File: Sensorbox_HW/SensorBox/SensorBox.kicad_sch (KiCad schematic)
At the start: 62 parts, among them Q1 BSS83P, SW1 SW_SPST, U1 BME280, U10 TLV2371D, U12 DS3231M, U2 LT1054, U3 PS1-O3-100, U4 MC33063AD, U6 MAX31855EASA, U8 HPP845E131R5, U9 TLV2371D

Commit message: Überarbeitung Sensorbox V3
Sicherheitsschaltung eingebaut, ESP anschauen warum getauscht, Email geschrieben
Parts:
- removed F1: Fuse, Fuse:Fuseholder_TR5_Littelfuse_No560_No460, symbol Device:Fuse
- removed SW1: SW_SPST, Button_Switch_THT:SW_SPST_Omron_B3F-40xx, symbol Switch:SW_SPST
- added LED1, LED2: rt, symbol Device:LED
- added Q2, Q3: BC327, Package_TO_SOT_THT:TO-92_Inline, symbol Transistor_BJT:BC327
- added R21, R22, R23: 1k, Resistor_SMD:R_0402_1005Metric, symbol Device:R
- added Rm: 5R, Resistor_SMD:R_0402_1005Metric, symbol Device:R
- MicroSD2: footprint (none) -> Connector_Card:microSD_HC_Molex_104031-0811
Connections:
- net GND1: no longer BT1.-
- net VCC_Bat: now also LED2.2 (A), Q2.1 (C)
- net at BT1.+: now also Q3.3 (E), Rm.2
- new net: BT1.-, R22.2, R23.2
- new net: LED1.2 (A), Q2.2 (B)
- new net: Q2.3 (E), R21.1, Rm.1
- new net: LED2.1 (K), R23.1
- new net: LED1.1 (K), Q3.1 (C), R22.1
- new net: Q3.2 (B), R21.2
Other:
- note added: "1V5 3x4V5 + Sicherung"
- note added: "RM = VBE/Ischwelle Rm=0,7V/0,140A =~5R"
- note added: "Sicherung +"
- note added: "Sicherung -"
- note removed: "1V5 3x 4V5"
- moved on the sheet: BT1, C1, C2, C3, C4, C5, C7, C8, CO1, CO2, CO3, CR1220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

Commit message: Überarbeitung V3
Besprechung mit B2 und einige Dinge Überarbeitet (Fuse, SD Card usw.)
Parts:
- removed JP2, JP3: Jumper_3_Bridged12, Connector_PinHeader_2.54mm:PinHeader_1x03_P2.54mm_Vertical, symbol Jumper:Jumper_3_Bridged12
- removed LED1, LED2: rt, symbol Device:LED
- removed Pulldown_Max2, Pulldown_Max318551, R1: 10k, Resistor_SMD:R_0402_1005Metric, symbol Device:R
- removed Q2, Q3: BC327, Package_TO_SOT_THT:TO-92_Inline, symbol Transistor_BJT:BC327
- removed R10, R9: 4.7k, Resistor_SMD:R_0402_1005Metric, symbol Device:R
- removed R16, R17, R18, R21, R22, R23: 1k, Resistor_SMD:R_0402_1005Metric, symbol Device:R
- removed Rm: 5R, Resistor_SMD:R_0402_1005Metric, symbol Device:R
- added ADC, GND1, SCL1, SDA/Signal1, VCC1: Conn_01x01_Socket, Connector_PinHeader_2.00mm:PinHeader_1x01_P2.00mm_Vertical, symbol Connector:Conn_01x01_Socket
- added C9: 100nF, Capacitor_SMD:C_0402_1005Metric_Pad0.74x0.62mm_HandSolder, symbol Device:C
- added D2, D3, D4: 1.5KExxA, Diode_THT:D_DO-201AE_P15.24mm_Horizontal, symbol Diode:1.5KExxA
- added F1: Polyfuse_Small, symbol Device:Polyfuse_Small
- added JP1: Jumper_2_Bridged, symbol Jumper:Jumper_2_Bridged
- CO2: value 00µF -> 10µF
- R19: value 2.2k -> 1k
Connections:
- net CS_GPIO5: now also MicroSD2.2 (CS), R21.1
- net GND1: now also BT1.-, U1.5 (SDO), C9.2, D2.2 (A2), D3.2 (A2), D4.2 (A2), GND1.1 (Pin_1); no longer R19.2, R20.2, R21.2, R7.2, R8.2
- net Mosi_GPIO23: now also MicroSD2.3 (DI), R20.1
- net RTC_32Khz_GPIO32: now also U7.5 (34); no longer U7.2 (EN)
- net SCK_GPIO18: now also MicroSD2.5 (SCK), R19.1
- net SCL_GPIO22: now also D2.1 (A1), SCL1.1 (Pin_1)
- net SDA_GPIO21: now also D4.1 (A1), SDA/Signal1.1 (Pin_1)
- net VCC_Bat: now also F1.2
- net VDD_3V3: now also R19.2, R20.2, R21.2, R7.2, R8.2; no longer U1.5 (SDO)
- net VDD_5V: now also C9.1, VCC1.1 (Pin_1)
- net at BT1.+: now also D3.1 (A1), F1.1
- net at U6.2 (T-): now also TH2.1, JP1.1 (A)
- net at TH2.2: now also U6.3 (T+), JP1.2 (B)
- net extern_Sensor_Gpio_32: now reaches U7.8 (33)
- net extern_Sensor_Gpio_32: now also ADC.1 (Pin_1)
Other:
- note added: "IoutMax bei -5V -> 100mA"
- note added: "Luftdruck-Sensor"
- note added: "Luftfeuchtigkeits-Sensor"
- note added: "Steckpins für den externen Sensor"
- note added: "Wichtig fürs Layout: Der Sensor der am Schluss der Datenleitung hängt Pullup Widerstände hängen. Hier BME!!!"
- note added: "für 3,3V"
- note removed: "BME280-Sensor"
- note removed: "Dauer --> P_BAT / P_Verbrauch = 46.06h"
- note removed: "HPP845E131R5-Sensor"
- note removed: "IoutMax bei -5V = 100mA"
- note removed: "P_Verbrauch = 0.122Wh"
- note removed: "RM = VBE/Ischwelle Rm=0,7V/0,140A =~5R"
- note removed: "Sicherung +"
- note removed: "Sicherung -"
- moved on the sheet: BT1

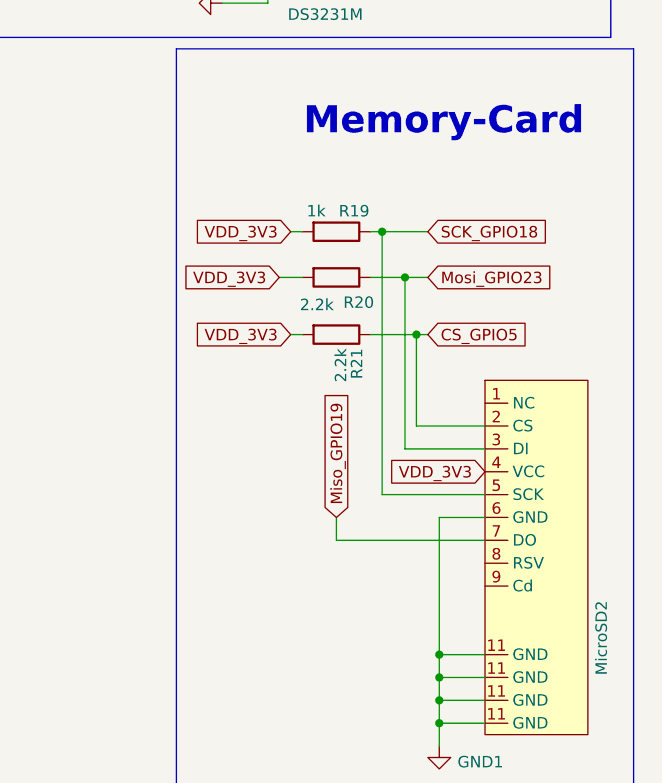
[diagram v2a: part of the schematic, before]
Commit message: Besprechung B2
Sicherung noch zu Datenleitungen dazu gehängt
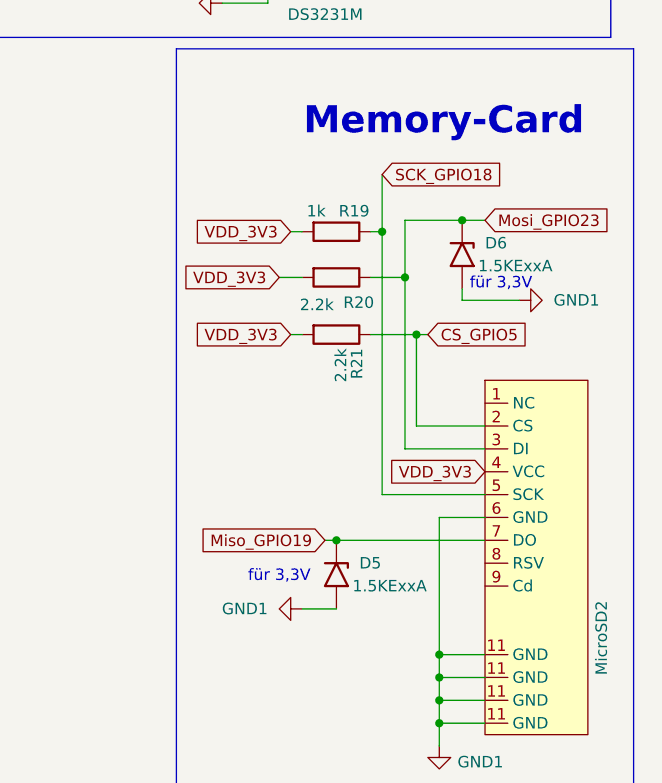
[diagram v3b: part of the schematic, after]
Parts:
- added D5, D6: 1.5KExxA, Diode_THT:D_DO-201AE_P15.24mm_Horizontal, symbol Diode:1.5KExxA
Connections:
- net GND1: now also D5.2 (A2), D6.2 (A2)
- net Miso_GPIO19: now also D5.1 (A1)
- net Mosi_GPIO23: now also D6.1 (A1)

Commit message: test
test
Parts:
- R19: value 1k -> 3k
- R20, R21: value 2.2k -> 3k
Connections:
- net RTC_32Khz_GPIO32 renamed RTC_32Khz_GPIO34
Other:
- note added: "Passt"
- note added: "Passt nicht"
- note added: "Passt nicht - EPAD anschauen ob es nötig ist"
- note added: "Passt nicht wegen Pin1"
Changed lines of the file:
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@@
 		)
 	)
+	(text "Passt"
+		(exclude_from_sim no)
+		(at 66.04 225.044 0)
+		(effects
+			(font
+				(size 2.032 2.032)
+				(thickness 0.4064)
+				(bold yes)
+			)
+		)
+	)
 	(text "Spannungsregler -- 3V-40V Input, Output\neinstellbar, hier indem Fall 5V"
 		(exclude_from_sim no)
@@
 		)
 	)
+	(text "Passt"
+		(exclude_from_sim no)
+		(at 268.732 172.72 0)
+		(effects
+			(font
+				(size 1.27 1.27)
+				(bold yes)
+			)
+		)
+	)
+	(text "Passt nicht wegen Pin1"
+		(exclude_from_sim no)
+		(at 387.35 52.07 0)
+		(effects
+			(font
+				(size 1.27 1.27)
+				(bold yes)
+			)
+		)
+	)
 	(text "für 3,3V\n"
 		(exclude_from_sim no)
@@
 		)
 	)
+	(text "Passt"
+		(exclude_from_sim no)
+		(at 196.596 24.384 0)
+		(effects
+			(font
+				(size 2.032 2.032)
+				(thickness 0.4064)
+				(bold yes)
+			)
+		)
+	)
 	(text "IoutMax bei -5V -> 100mA\n"
 		(exclude_from_sim no)
@@
 		)
 	)
+	(text "Passt\n"
+		(exclude_from_sim no)
+		(at 248.412 150.876 0)
+		(effects
+			(font
+				(size 1.27 1.27)
+				(bold yes)
+			)
+		)
+	)
 	(text "Spannungs Inverter\n"
 		(exclude_from_sim no)
@@
 		)
 	)
+	(text "Passt nicht "
+		(exclude_from_sim no)
+		(at 366.522 143.002 0)
+		(effects
+			(font
+				(size 1.27 1.27)
+				(bold yes)
+			)
+		)
+	)
+	(text "Passt nicht - EPAD anschauen \nob es nötig ist"
+		(exclude_from_sim no)
+		(at 135.89 179.578 0)
+		(effects
+			(font
+				(size 1.27 1.27)
+				(bold yes)
+			)
+		)
+	)
 	(text "Ozon-Sensor"
 		(exclude_from_sim no)
@@
 		)
 	)
+	(text "Passt nicht"
+		(exclude_from_sim no)
+		(at 176.276 175.26 0)
+		(effects
+			(font
+				(size 1.27 1.27)
+				(bold yes)
+			)
+		)
+	)
+	(text "Passt"
+		(exclude_from_sim no)
+		(at 175.26 88.9 0)
+		(effects
+			(font
+				(size 2.032 2.032)
+				(thickness 0.4064)
+				(bold yes)
+			)
+		)
+	)
 	(global_label "VDD_3V3"
 		(shape input)
@@
 		)
 	)
-	(global_label "RTC_32Khz_GPIO32"
+	(global_label "RTC_32Khz_GPIO34"
 		(shape input)
 		(at 255.27 39.37 180)
@@
 		)
 	)
-	(global_label "RTC_32Khz_GPIO32"
+	(global_label "RTC_32Khz_GPIO34"
 		(shape input)
 		(at 378.46 35.56 0)
@@
 			)
 		)
-		(property "Value" "2.2k"
+		(property "Value" "3k"
 			(at 365.506 85.598 90)
 			(effects
@@
 			)
 		)
-		(property "Value" "1k"
+		(property "Value" "3k"
 			(at 366.268 75.184 90)
 			(effects
@@
 			)
 		)
-		(property "Value" "2.2k"
+		(property "Value" "3k"
 			(at 370.078 90.424 0)
 			(effects

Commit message: SensorboxV4
Fertigstellen
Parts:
- removed C3, C7: 100nF, Capacitor_SMD:C_0402_1005Metric_Pad0.74x0.62mm_HandSolder, symbol Device:C
- removed CO1: 2µF, Capacitor_SMD:C_0402_1005Metric_Pad0.74x0.62mm_HandSolder, symbol Device:C
- removed CO2: 10µF, Capacitor_SMD:C_0402_1005Metric_Pad0.74x0.62mm_HandSolder, symbol Device:C
- removed CO3: 100µF, Capacitor_SMD:C_0402_1005Metric_Pad0.74x0.62mm_HandSolder, symbol Device:C
- removed Q1: BSS83P, Package_TO_SOT_SMD:SOT-23, symbol Transistor_FET:BSS83P
- removed R11, R2, R3: 10k, Resistor_SMD:R_0402_1005Metric, symbol Device:R
- removed R4, R5: 10R, Resistor_SMD:R_0402_1005Metric, symbol Device:R
- removed R6: 100k, Resistor_SMD:R_0402_1005Metric, symbol Device:R
- removed RGain: 82k, Resistor_SMD:R_0402_1005Metric, symbol Device:R
- removed U10, U9: TLV2371D, Package_SO:SOIC-8_3.9x4.9mm_P1.27mm, symbol Amplifier_Operational:TLV2371D
- removed U2: LT1054, symbol Regulator_SwitchedCapacitor:LT1054
- removed U3: PS1-O3-100, PS1O3100, symbol PS1-O3-100:PS1-O3-100
- added C10, C11, C12, CO4: 100nF, Capacitor_SMD:C_0402_1005Metric_Pad0.74x0.62mm_HandSolder, symbol Device:C
- added R1: 10R, Resistor_SMD:R_0402_1005Metric, symbol Device:R
- added R10, R18, R19, R1_6, R9: 10kR, Resistor_SMD:R_0402_1005Metric, symbol Device:R
- added R1_1, Rset1: 10k, Resistor_SMD:R_0402_1005Metric, symbol Device:R
- added R1_2: 0R, Resistor_SMD:R_0402_1005Metric, symbol Device:R
- added R1_3: 1.3 kR, Resistor_SMD:R_0402_1005Metric, symbol Device:R
- added R1_4, R1_5: 1kR, Resistor_SMD:R_0402_1005Metric, symbol Device:R
- added TP1, TP10, TP11, TP2, TP3, TP4, TP5, TP6, TP7, TP8, TP9: TestPoint, TestPoint:TestPoint_Loop_D1.80mm_Drill1.0mm_Beaded, symbol Connector:TestPoint
- added U11: PS1-O3-100, PS1O3100, symbol PS1-O3-100:PS1-O3-100
- added U13, U2, U5: OPA197xD, Package_SO:SOIC-8_3.9x4.9mm_P1.27mm, symbol Amplifier_Operational:OPA197xD
- renumbered ADC to ADC1, CO to CO1, CT to CT1, R1_ to R1_7, R2_ to R2_1, R19 to R33, Rsc to Rsc1, Rx to Rx1
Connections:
- net GND1: now also U8.7 (EPAD), C10.2, CO4.1, R1_5.1, R1_6.1, U13.4 (V-), U2.4 (V-), U5.4 (V-)
- net Mosi_GPIO23: now also TP5.1
- net RTC_INIT_GPIO4: now also TP7.1
- net SCL_GPIO22: now also TP6.1
- net VCC_Bat: now also TP3.1
- net VDD_3V3: now also C10.1, CO4.2, R1_1.1, TP4.1, TP8.1, TP9.1, U2.7 (V+)
- net VDD_5V: now also R1_4.2, TP2.1, U13.7 (V+), U5.7 (V+)
- net Ozon_out_ADC_GPIO27: now reaches U7.11 (27)
- net Ozon_out_ADC_GPIO27: now also R1_2.1, TP1.1
- net at U7.2 (EN): now also R1_1.2
- net RTC_32Khz_GPIO25: now reaches U7.9 (25)
- net RTC_32Khz_GPIO25: now also R15.2, U12.1 (32KHZ)
- net Ozon_out_Gpio35: no longer names the net of U7.6 (35)
- removed net RTC_32Khz_GPIO34: R15.2, U12.1 (32KHZ), U7.5 (34)
- net extern_Sensor_Gpio_32 renamed extern_Sensor_Gpio_33
- new net: R19.1, U11.R1
- new net: C11.2, R18.1, R19.2
- new net: R9.1, U13.3 (+)
- new net: R1_4.1, R1_5.2, U2.3 (+)
- new net: R18.2, U5.2 (-)
- new net: C12.2, R10.1, R1_2.2, U13.6
- new net: C12.1, R1.1, R10.2, U13.2 (-)
- new net: R1.2, U11.S1
- new net: C11.1, U11.C1, U5.6
- new net: R1_3.1, R1_6.2, Rset1.2, TP11.1
- new net: Rset1.1, U5.3 (+)
- new net VDD_2.5V: R1_3.2, R9.2, TP10.1, U2.2 (-), U2.6
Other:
- note added: "2,5V"
- note added: "2.2V"
- note added: "Wir verwenden den OPA197 als Impedanzwandler, damit die 2,5V-Referenzspannung stabil bleibt, da ohne ihn die Spannung durch die Belastung des nachfolgenden Schaltungsteils absinken könnte."
- note removed: "IoutMax bei -5V -> 100mA"
- note removed: "Spannungs Inverter"
- moved on the sheet: C1, C2, C4, R7, R8, U1, U8

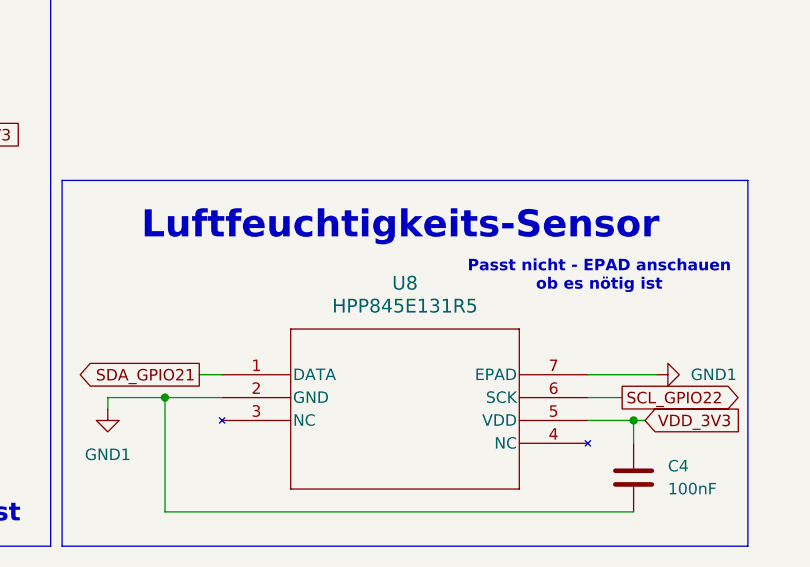
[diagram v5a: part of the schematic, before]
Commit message: changes hw
problems with sch.
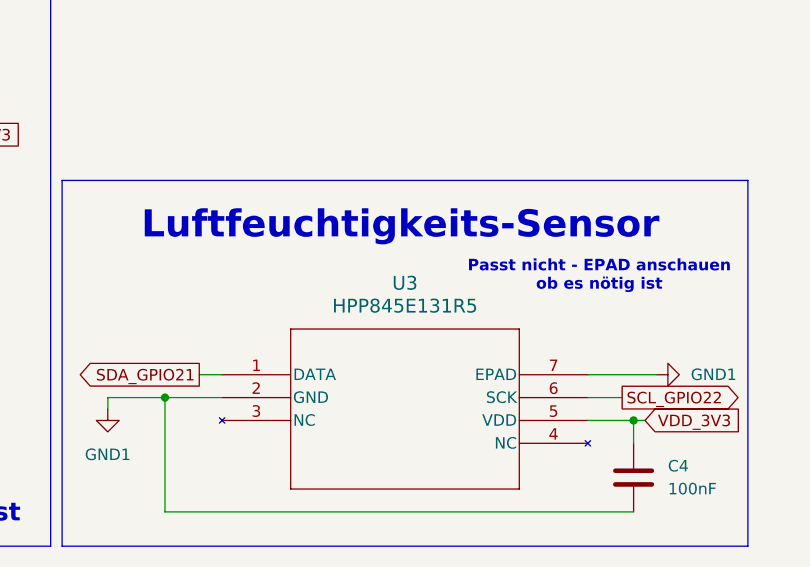
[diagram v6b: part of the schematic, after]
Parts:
- removed U8: HPP845E131R5, HPP845E131R5:SON6_HPP845E131R5_TEC, symbol HPP845E131R5:HPP845E131R5
- added U3: HPP845E131R5, HPP_footprints:SON6_HPP845E131R5_TEC, symbol 2024-10-21_12-55-34:HPP845E131R5
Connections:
- net GND1: now also U3.2 (GND), U3.7 (EPAD)
- net SCL_GPIO22: now also U3.6 (SCK)
- net SDA_GPIO21: now also U3.1 (DATA)
- net VDD_3V3: now also U3.5 (VDD)
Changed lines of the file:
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@@
 		)
 		(instances
-			(project ""
+			(project "SensorBox"
 				(path "/7cbe8151-7294-42e6-9c4e-6ec8952d674f"
 					(reference "CR1220")
@@
 		)
 		(instances
-			(project ""
+			(project "SensorBox"
 				(path "/7cbe8151-7294-42e6-9c4e-6ec8952d674f"
 					(reference "TP1")
@@
 		)
 		(instances
-			(project ""
+			(project "SensorBox"
 				(path "/7cbe8151-7294-42e6-9c4e-6ec8952d674f"
 					(reference "F1")
@@
 	)
 	(symbol
+		(lib_id "2024-10-21_12-55-34:HPP845E131R5")
+		(at 95.25 170.18 0)
+		(unit 1)
+		(exclude_from_sim no)
+		(in_bom yes)
+		(on_board yes)
+		(dnp no)
+		(fields_autoplaced yes)
+		(property "Reference" "U3"
+			(at 115.57 160.02 0)
+			(effects
+				(font
+					(size 1.524 1.524)
+				)
+			)
+		)
+		(property "Value" "HPP845E131R5"
+			(at 115.57 162.56 0)
+			(effects
+				(font
+					(size 1.524 1.524)
+				)
+			)
+		)
+		(property "Footprint" "HPP_footprints:SON6_HPP845E131R5_TEC"
+			(at 95.25 170.18 0)
+			(effects
+				(font
+					(size 1.27 1.27)
+					(italic yes)
+				)
+				(hide yes)
+			)
+		)
+		(property "Datasheet" "HPP845E131R5"
+			(at 95.25 170.18 0)
+			(effects
+				(font
+					(size 1.27 1.27)
+					(italic yes)
+				)
+				(hide yes)
+			)
+		)
+		(property "Description" ""
+			(at 95.25 170.18 0)
+			(effects
+				(font
+					(size 1.27 1.27)
+				)
+				(hide yes)
+			)
+		)
+		(pin "2"
+		)
+		(pin "1"
+		)
+		(pin "7"
+		)
+		(pin "5"
+		)
+		(pin "3"
+		)
+		(pin "4"
+		)
+		(pin "6"
+		)
+		(instances
+			(project "SensorBox"
+				(path "/7cbe8151-7294-42e6-9c4e-6ec8952d674f"
+					(reference "U3")
+					(unit 1)
+				)
+			)
+		)
+	)
+	(symbol
 		(lib_id "Device:R")
 		(at 36.83 34.29 0)
@@
 		)
 		(instances
-			(project ""
+			(project "SensorBox"
 				(path "/7cbe8151-7294-42e6-9c4e-6ec8952d674f"
 					(reference "JP1")
@@
 		)
 		(instances
-			(project ""
+			(project "SensorBox"
 				(path "/7cbe8151-7294-42e6-9c4e-6ec8952d674f"
 					(reference "U12")
@@
 		)
 		(instances
-			(project ""
+			(project "SensorBox"
 				(path "/7cbe8151-7294-42e6-9c4e-6ec8952d674f"
 					(reference "MicroSD2")
@@
 		)
 		(instances
-			(project ""
+			(project "SensorBox"
 				(path "/7cbe8151-7294-42e6-9c4e-6ec8952d674f"
 					(reference "D3")
@@
 	)
 	(symbol
-		(lib_name "HPP845E131R5_1")
-		(lib_id "HPP845E131R5:HPP845E131R5")
-		(at 95.25 170.18 0)
-		(unit 1)
-		(exclude_from_sim no)
-		(in_bom yes)
-		(on_board yes)
-		(dnp no)
-		(fields_autoplaced yes)
-		(property "Reference" "U8"
-			(at 115.57 160.02 0)
-			(effects
-				(font
-					(size 1.524 1.524)
-				)
-			)
-		)
-		(property "Value" "HPP845E131R5"
-			(at 115.57 162.56 0)
-			(effects
-				(font
-					(size 1.524 1.524)
-				)
-			)
-		)
-		(property "Footprint" "HPP845E131R5:SON6_HPP845E131R5_TEC"
-			(at 95.25 170.18 0)
-			(effects
-				(font
-					(size 1.27 1.27)
-					(italic yes)
-				)
-				(hide yes)
-			)
-		)
-		(property "Datasheet" "https://www.mouser.at/datasheet/2/418/5/NG_DS_HPC199_6_A6-1130111.pdf"
-			(at 95.25 170.18 0)
-			(effects
-				(font
-					(size 1.27 1.27)
-					(italic yes)
-				)
-				(hide yes)
-			)
-		)
-		(property "Description" ""
-			(at 95.25 170.18 0)
-			(effects
-				(font
-					(size 1.27 1.27)
-				)
-				(hide yes)
-			)
-		)
-		(pin "3"
-		)
-		(pin "2"
-		)
-		(pin "1"
-		)
-		(pin "7"
-		)
-		(pin "6"
-		)
-		(pin "5"
-		)
-		(pin "4"
-		)
-		(instances
-			(project "SensorBox"
-				(path "/7cbe8151-7294-42e6-9c4e-6ec8952d674f"
-					(reference "U8")
-					(unit 1)
-				)
-			)
-		)
-	)
-	(symbol
 		(lib_id "Connector:TestPoint")
 		(at 152.4 44.45 0)
@@
 		)
 		(instances
-			(project ""
+			(project "SensorBox"
 				(path "/7cbe8151-7294-42e6-9c4e-6ec8952d674f"
 					(reference "U7")
@@
 		)
 		(instances
-			(project ""
+			(project "SensorBox"
 				(path "/7cbe8151-7294-42e6-9c4e-6ec8952d674f"
 					(reference "U5")
